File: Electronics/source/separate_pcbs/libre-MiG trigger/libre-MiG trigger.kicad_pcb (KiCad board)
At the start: 2 copper layers, 18 x 35 mm, 6 parts, among them J18 Conn_01x03, SW2 SW_Push, SW3 SW_Push

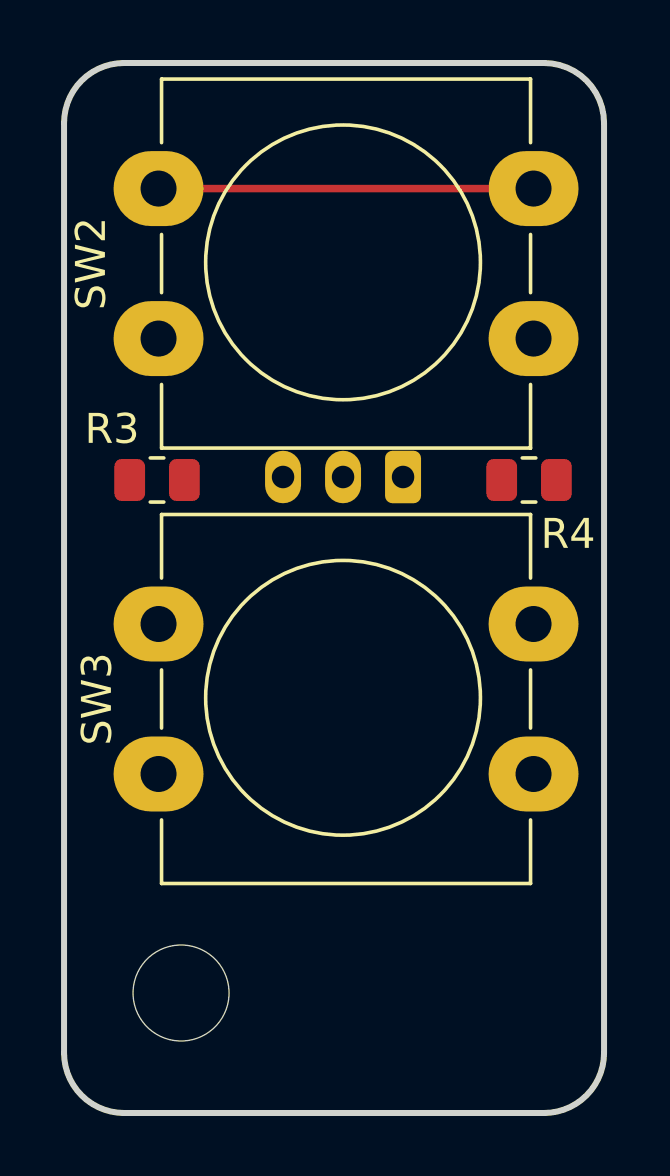
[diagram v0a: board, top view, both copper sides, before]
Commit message: added mechanical ignore
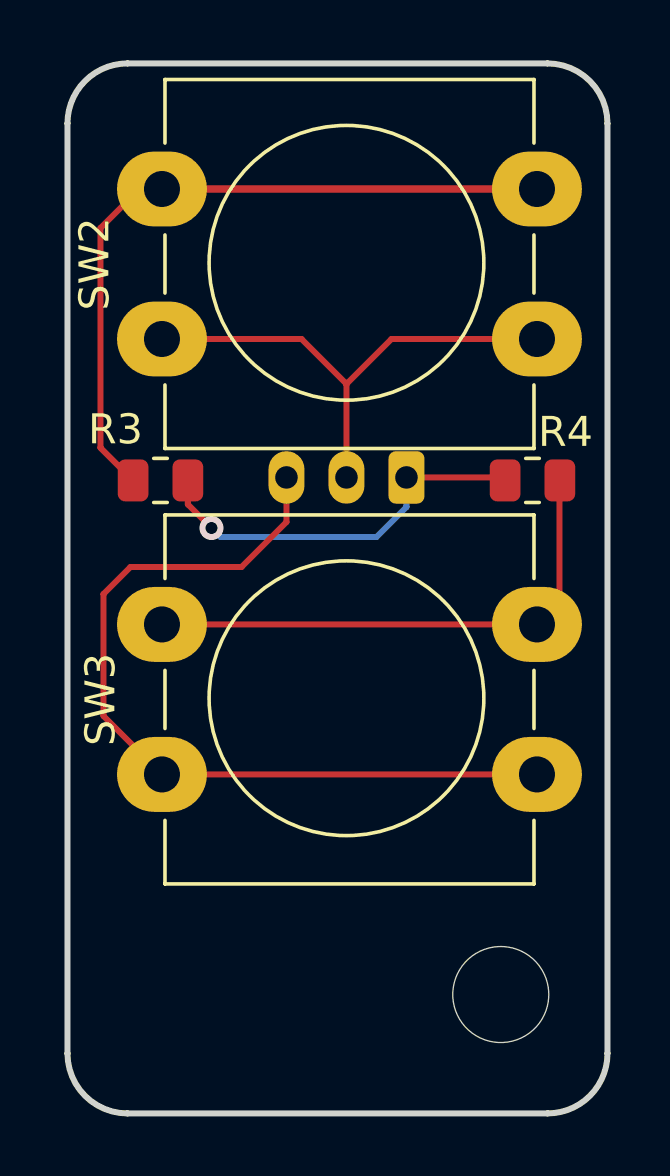
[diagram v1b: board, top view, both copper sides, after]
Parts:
- moved REF** 10.7 mm to (121.1, 186.0)
- moved R3 0.12 mm to (109.8, 168.9)
- moved J18 0.12 mm to (118.0, 168.8)
- moved R4 0.12 mm to (122.2, 168.9), turned to 0 degrees
- moved SW2 0.12 mm to (122.3, 164.1)
- moved SW3 0.12 mm to (122.3, 178.7)
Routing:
- net /Trigger/Stage2: track 0.00 -> 27.9 mm
- net Net-(R4-Pad2): track 0.00 -> 17.6 mm
- net /Trigger/Stage1: track 0.00 -> 16.9 mm
- net +3V3: track 0.00 -> 13.3 mm, vias 0 -> 1
- net Net-(R3-Pad2): track 12.5 -> 24.0 mm
